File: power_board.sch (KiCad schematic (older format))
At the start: 26 parts, among them J1 Conn_01x01, J10 Conn_01x01, J11 Conn_01x01, J12 Conn_01x01, J13 Conn_01x01, J14 Conn_01x01, J15 Conn_01x01, J16 Conn_01x01, J2 Conn_01x01, J3 Conn_01x01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

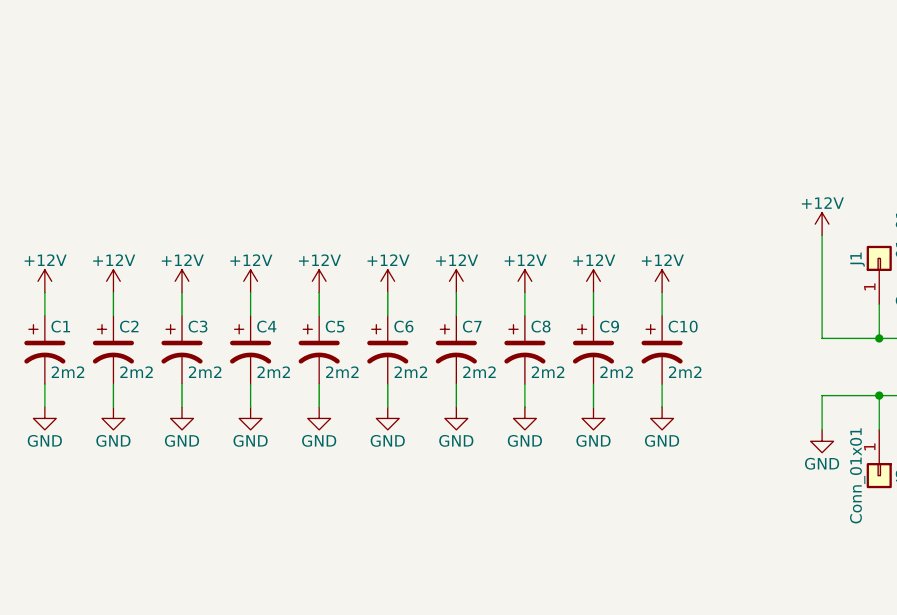
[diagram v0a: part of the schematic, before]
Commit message: add MPN and change footprints
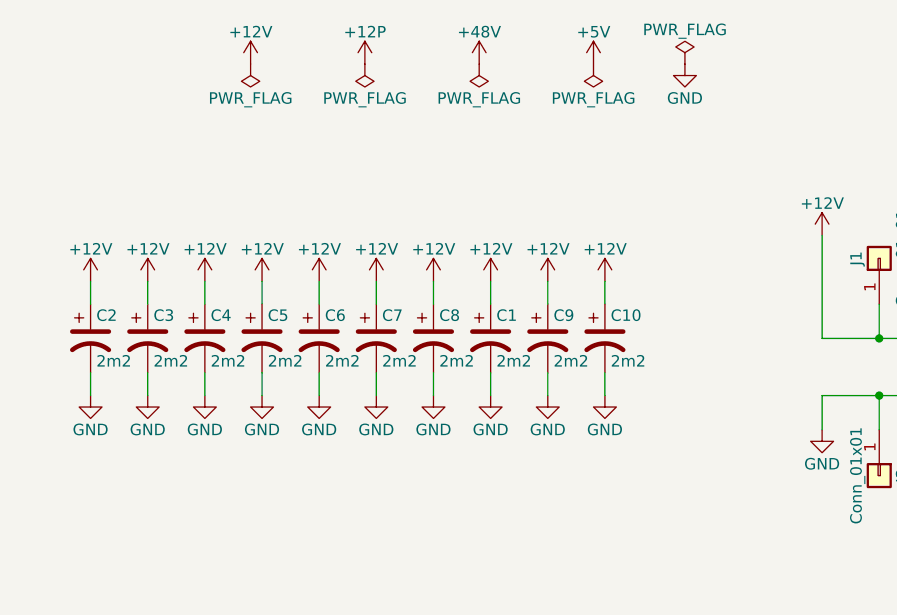
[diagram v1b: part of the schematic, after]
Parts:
- C1: footprint Capacitor_THT:CP_Radial_D10.0mm_P5.00mm -> Capacitor_THT:CP_Radial_D12.5mm_P5.00mm; MPN 565-4315-ND -> 2313329
- C10, C8: footprint Capacitor_THT:CP_Radial_D10.0mm_P5.00mm -> Capacitor_THT:CP_Radial_D12.5mm_P5.00mm; MPN (none) -> 2313329; note 3228 -> (none)
- C2, C3, C5, C6, C7, C9: footprint Capacitor_THT:CP_Radial_D10.0mm_P5.00mm -> Capacitor_THT:CP_Radial_D12.5mm_P5.00mm; MPN (none) -> 2313329
- C4: footprint Capacitors_THT:CP_Radial_D35.0mm_P10.00mm_SnapIn -> Capacitor_THT:CP_Radial_D12.5mm_P5.00mm; MPN (none) -> 2313329; note 3228 -> (none)
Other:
- moved on the sheet: C1

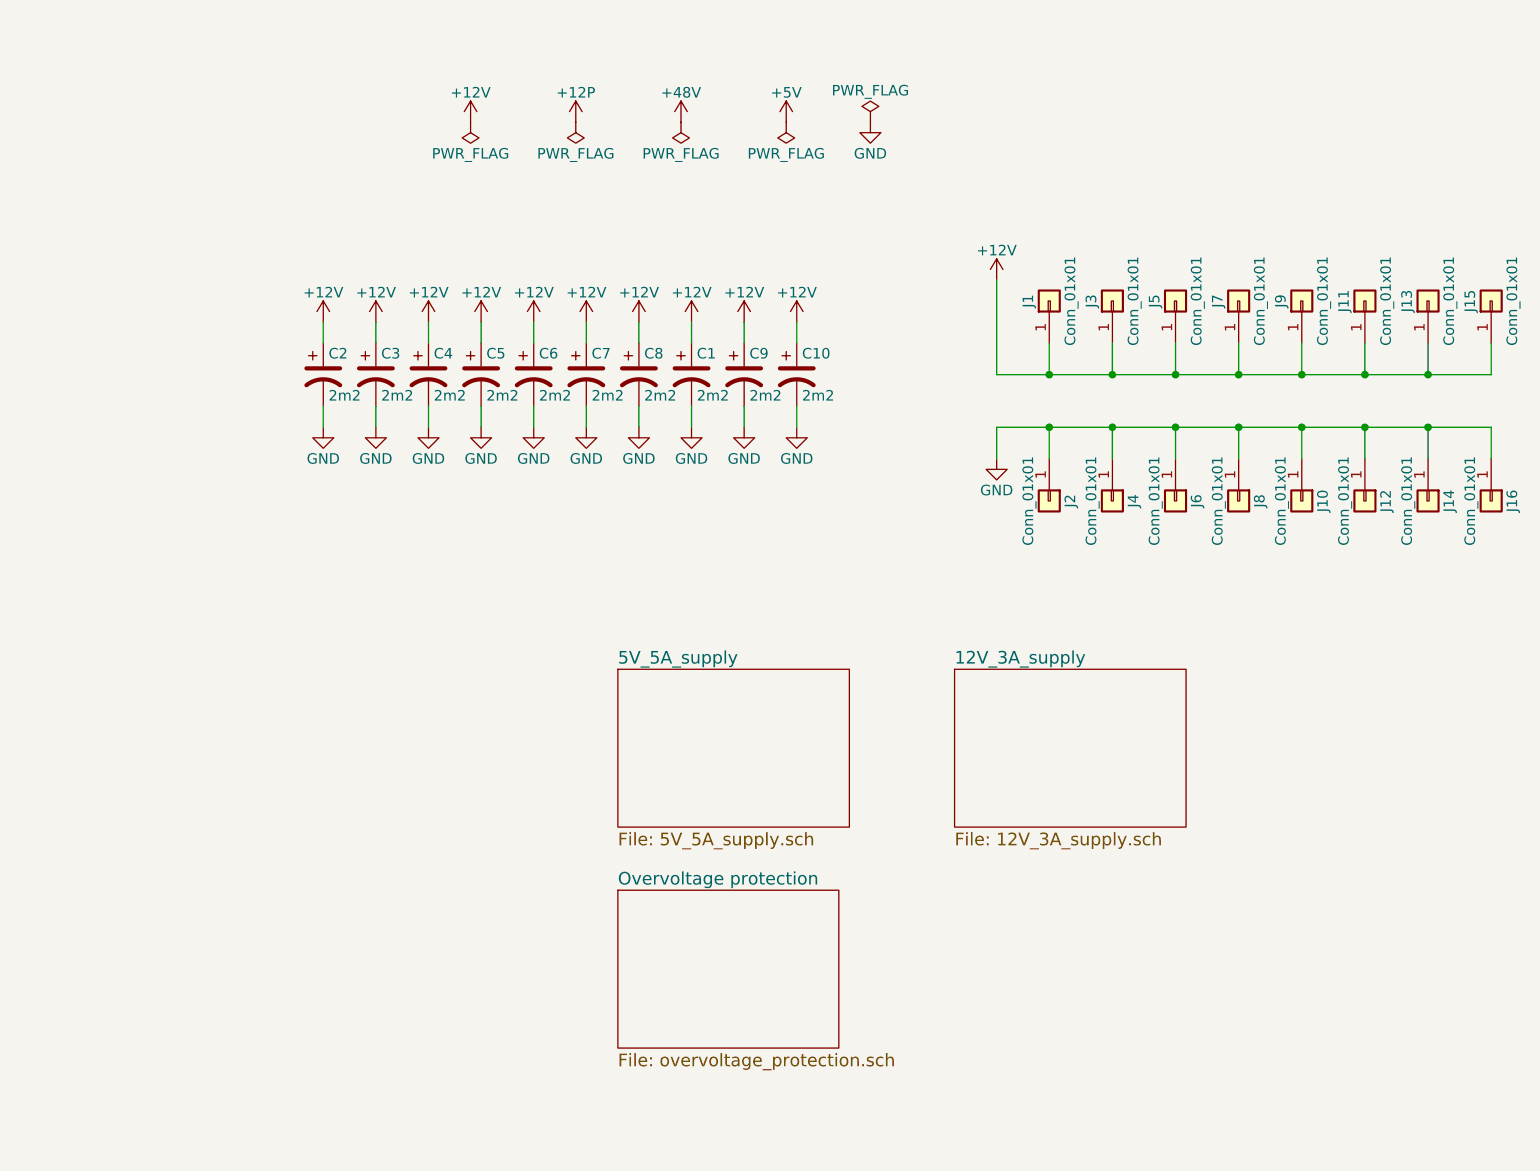
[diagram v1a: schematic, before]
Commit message: 12v 3x_conn added
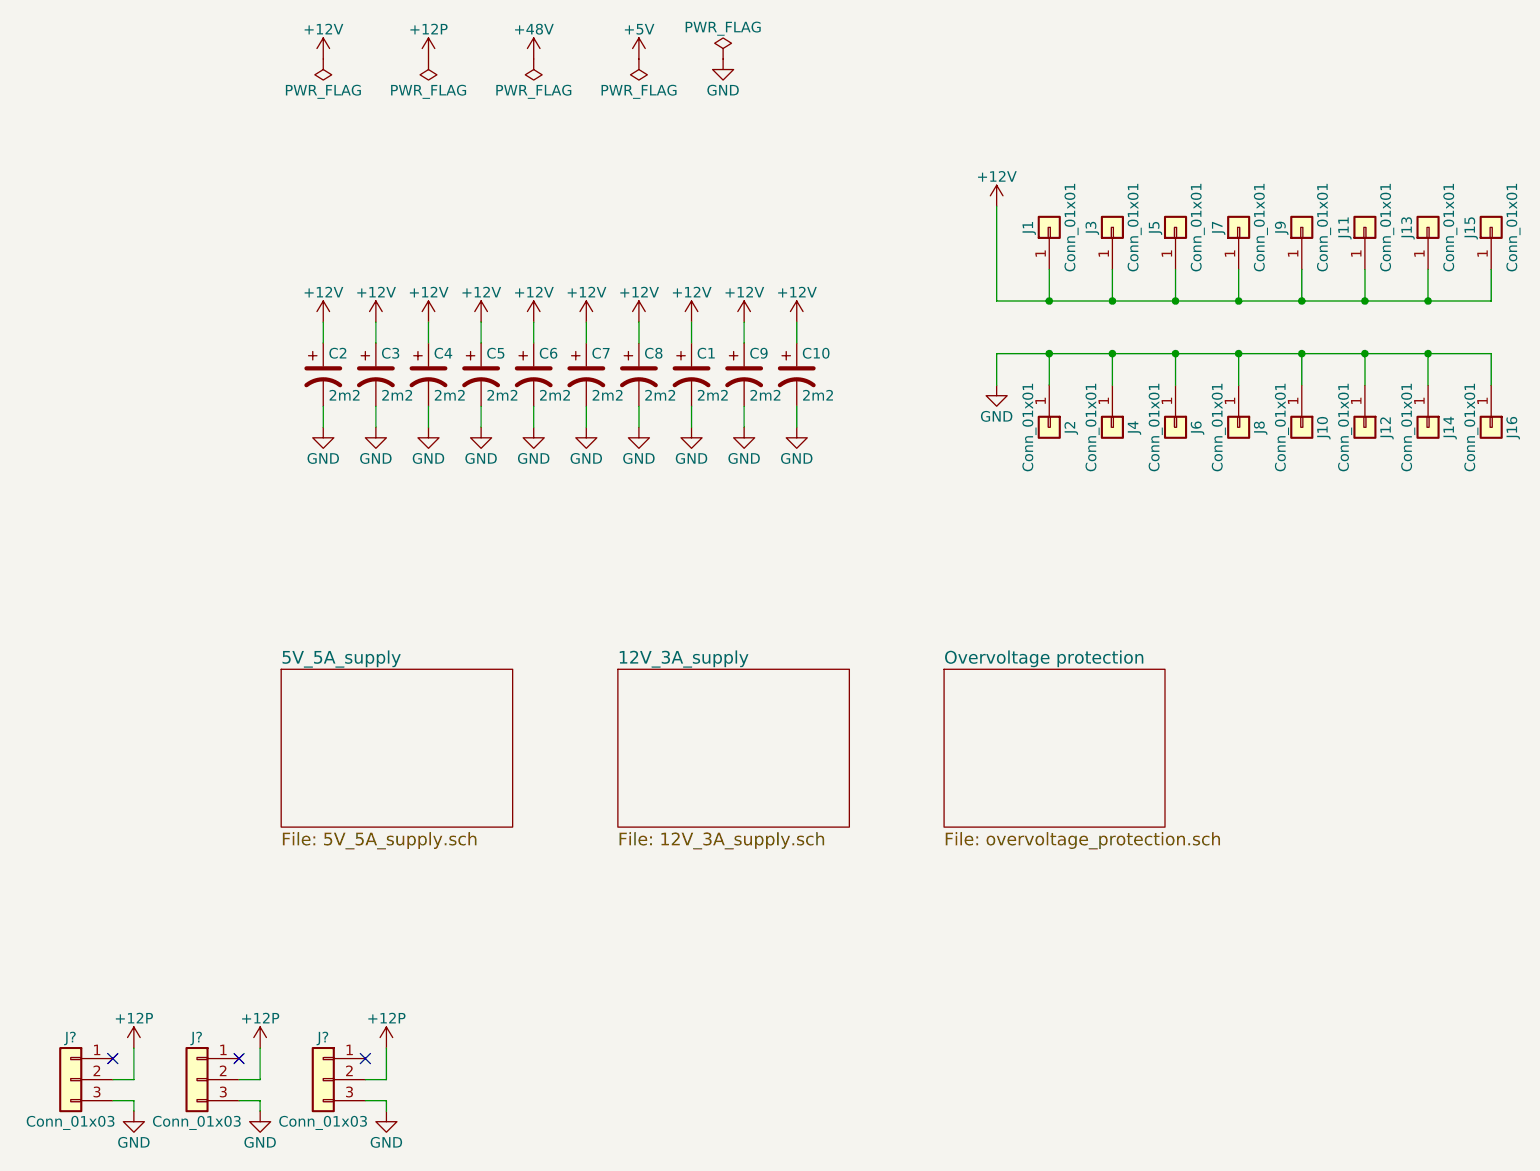
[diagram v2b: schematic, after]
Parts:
- added J? (x3): Conn_01x03, Connector_Molex:Molex_CLIK-Mate_502382-0370_1x03_P1.25mm_Vertical, symbol Conn_01x03
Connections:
- net +12P: now also J?.2 (Pin_2), J?.2 (Pin_2), J?.2 (Pin_2)
- net GND: now also J?.3 (Pin_3), J?.3 (Pin_3), J?.3 (Pin_3)
- no-connect marks 0 -> 3
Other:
- moved on the sheet: J1, J10, J11, J12, J13, J14, J15, J16, J2, J3, J4, J5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

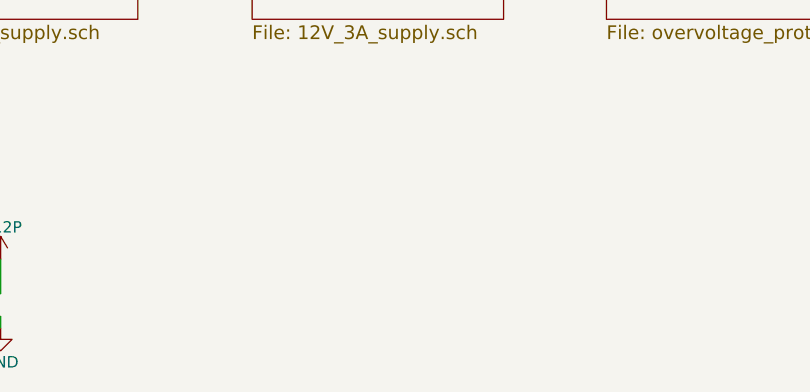
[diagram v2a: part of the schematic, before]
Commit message: mpn was changed
added needed conectors
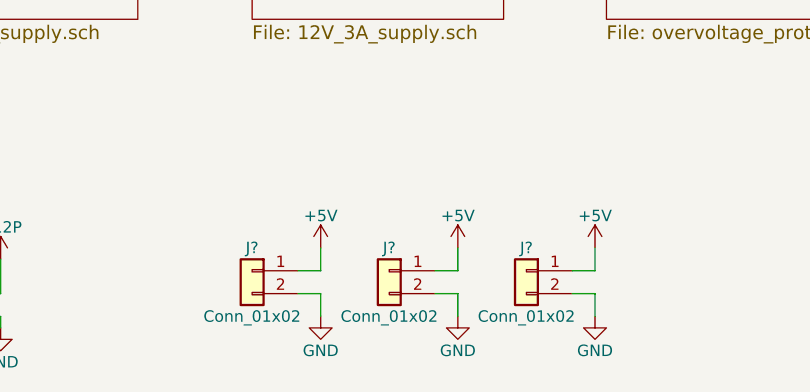
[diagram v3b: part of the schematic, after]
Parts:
- added J? (x3): Conn_01x02, Connector_JST:JST_EH_S02B-EH_1x02_P2.50mm_Horizontal, symbol Conn_01x02
- C1, C10, C2, C3, C4, C5, C6, C7, C8, C9: MPN 2313329 -> EEUFR1C222B
- J? (x3): footprint Connector_Molex:Molex_CLIK-Mate_502382-0370_1x03_P1.25mm_Vertical -> Connector_Molex:Molex_Panelmate_53780-0370_1x03_P1.25mm_Horizontal; MPN 1125359 -> 53261-0371
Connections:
- net +5V: now also J?.1 (Pin_1), J?.1 (Pin_1), J?.1 (Pin_1)
- net GND: now also J?.2 (Pin_2), J?.2 (Pin_2), J?.2 (Pin_2)
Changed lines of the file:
@@
 F 2 "Capacitor_THT:CP_Radial_D12.5mm_P5.00mm" H 4650 2650 50  0001 C CNN
 F 3 "" H 4650 2650 50  0001 C CNN
-F 4 "2313329" H 4650 2650 60  0001 C CNN "MPN"
+F 4 "EEUFR1C222B" H 4650 2650 60  0001 C CNN "MPN"
 	1    4650 2650
 	1    0    0    -1
@@
 F 2 "Capacitor_THT:CP_Radial_D12.5mm_P5.00mm" H 4400 2650 50  0001 C CNN
 F 3 "" H 4400 2650 50  0001 C CNN
-F 4 "2313329" H 4400 2650 60  0001 C CNN "MPN"
+F 4 "EEUFR1C222B" H 4400 2650 60  0001 C CNN "MPN"
 	1    4400 2650
 	1    0    0    -1
@@
 F 2 "Capacitor_THT:CP_Radial_D12.5mm_P5.00mm" H 4150 2650 50  0001 C CNN
 F 3 "" H 4150 2650 50  0001 C CNN
-F 4 "2313329" H 4150 2650 60  0001 C CNN "MPN"
+F 4 "EEUFR1C222B" H 4150 2650 60  0001 C CNN "MPN"
 	1    4150 2650
 	1    0    0    -1
@@
 F 2 "Capacitor_THT:CP_Radial_D12.5mm_P5.00mm" H 3900 2650 50  0001 C CNN
 F 3 "" H 3900 2650 50  0001 C CNN
-F 4 "2313329" H 3900 2650 60  0001 C CNN "MPN"
+F 4 "EEUFR1C222B" H 3900 2650 60  0001 C CNN "MPN"
 	1    3900 2650
 	1    0    0    -1
@@
 F 2 "Capacitor_THT:CP_Radial_D12.5mm_P5.00mm" H 3650 2650 50  0001 C CNN
 F 3 "" H 3650 2650 50  0001 C CNN
-F 4 "2313329" H 3650 2650 60  0001 C CNN "MPN"
+F 4 "EEUFR1C222B" H 3650 2650 60  0001 C CNN "MPN"
 	1    3650 2650
 	1    0    0    -1
@@
 F 2 "Capacitor_THT:CP_Radial_D12.5mm_P5.00mm" H 3400 2650 50  0001 C CNN
 F 3 "" H 3400 2650 50  0001 C CNN
-F 4 "2313329" H 3400 2650 60  0001 C CNN "MPN"
+F 4 "EEUFR1C222B" H 3400 2650 60  0001 C CNN "MPN"
 	1    3400 2650
 	1    0    0    -1
@@
 F 2 "Capacitor_THT:CP_Radial_D12.5mm_P5.00mm" H 3150 2650 50  0001 C CNN
 F 3 "" H 3150 2650 50  0001 C CNN
-F 4 "2313329" H 3150 2650 60  0001 C CNN "MPN"
+F 4 "EEUFR1C222B" H 3150 2650 60  0001 C CNN "MPN"
 	1    3150 2650
 	1    0    0    -1
@@
 F 2 "Capacitor_THT:CP_Radial_D12.5mm_P5.00mm" H 2900 2650 50  0001 C CNN
 F 3 "" H 2900 2650 50  0001 C CNN
-F 4 "2313329" H 2900 2650 60  0001 C CNN "MPN"
+F 4 "EEUFR1C222B" H 2900 2650 60  0001 C CNN "MPN"
 	1    2900 2650
 	1    0    0    -1
@@
 F 2 "Capacitor_THT:CP_Radial_D12.5mm_P5.00mm" H 5150 2650 50  0001 C CNN
 F 3 "" H 5150 2650 50  0001 C CNN
-F 4 "2313329" H 5150 2650 60  0001 C CNN "MPN"
+F 4 "EEUFR1C222B" H 5150 2650 60  0001 C CNN "MPN"
 	1    5150 2650
 	1    0    0    -1
@@
 F 2 "Capacitor_THT:CP_Radial_D12.5mm_P5.00mm" H 4900 2650 50  0001 C CNN
 F 3 "" H 4900 2650 50  0001 C CNN
-F 4 "2313329" H 4900 2650 60  0001 C CNN "MPN"
+F 4 "EEUFR1C222B" H 4900 2650 60  0001 C CNN "MPN"
 	1    4900 2650
 	1    0    0    -1
@@
 F 0 "J?" H 1700 6200 50  0000 C CNN
 F 1 "Conn_01x03" H 1700 5800 50  0000 C CNN
-F 2 "Connector_Molex:Molex_CLIK-Mate_502382-0370_1x03_P1.25mm_Vertical" H 1700 6000 50  0001 C CNN
+F 2 "Connector_Molex:Molex_Panelmate_53780-0370_1x03_P1.25mm_Horizontal" H 1700 6000 50  0001 C CNN
 F 3 "" H 1700 6000 50  0001 C CNN
-F 4 "1125359" H 1700 6000 60  0001 C CNN "MPN"
+F 4 "53261-0371" H 1700 6000 60  0001 C CNN "MPN"
 	1    1700 6000
 	-1   0    0    -1
@@
 F 0 "J?" H 2300 6200 50  0000 C CNN
 F 1 "Conn_01x03" H 2300 5800 50  0000 C CNN
-F 2 "Connector_Molex:Molex_CLIK-Mate_502382-0370_1x03_P1.25mm_Vertical" H 2300 6000 50  0001 C CNN
+F 2 "Connector_Molex:Molex_Panelmate_53780-0370_1x03_P1.25mm_Horizontal" H 2300 6000 50  0001 C CNN
 F 3 "" H 2300 6000 50  0001 C CNN
-F 4 "1125359" H 2300 6000 60  0001 C CNN "MPN"
+F 4 "53261-0371" H 2300 6000 60  0001 C CNN "MPN"
 	1    2300 6000
 	-1   0    0    -1
@@
 F 0 "J?" H 2900 6200 50  0000 C CNN
 F 1 "Conn_01x03" H 2900 5800 50  0000 C CNN
-F 2 "Connector_Molex:Molex_CLIK-Mate_502382-0370_1x03_P1.25mm_Vertical" H 2900 6000 50  0001 C CNN
+F 2 "Connector_Molex:Molex_Panelmate_53780-0370_1x03_P1.25mm_Horizontal" H 2900 6000 50  0001 C CNN
 F 3 "" H 2900 6000 50  0001 C CNN
-F 4 "1125359" H 2900 6000 60  0001 C CNN "MPN"
+F 4 "53261-0371" H 2900 6000 60  0001 C CNN "MPN"
 	1    2900 6000
 	-1   0    0    -1
@@
 Wire Wire Line
 	3200 6100 3200 6150
+$Comp
+L Conn_01x02 J?
+U 1 1 5AB13823
+P 4300 5900
+F 0 "J?" H 4300 6000 50  0000 C CNN
+F 1 "Conn_01x02" H 4300 5700 50  0000 C CNN
+F 2 "Connector_JST:JST_EH_S02B-EH_1x02_P2.50mm_Horizontal" H 4300 5900 50  0001 C CNN
+F 3 "" H 4300 5900 50  0001 C CNN
+F 4 "S2B-EH(LF)(SN)" H 4300 5900 60  0001 C CNN "MPN"
+	1    4300 5900
+	-1   0    0    -1
+$EndComp
+$Comp
+L GND #PWR?
+U 1 1 5AB13AC1
+P 4600 6100
+F 0 "#PWR?" H 4600 5850 50  0001 C CNN
+F 1 "GND" H 4600 5950 50  0000 C CNN
+F 2 "" H 4600 6100 50  0001 C CNN
+F 3 "" H 4600 6100 50  0001 C CNN
+	1    4600 6100
+	1    0    0    -1
+$EndComp
+$Comp
+L GND #PWR?
+U 1 1 5AB13B2C
+P 5200 6100
+F 0 "#PWR?" H 5200 5850 50  0001 C CNN
+F 1 "GND" H 5200 5950 50  0000 C CNN
+F 2 "" H 5200 6100 50  0001 C CNN
+F 3 "" H 5200 6100 50  0001 C CNN
+	1    5200 6100
+	1    0    0    -1
+$EndComp
+$Comp
+L GND #PWR?
+U 1 1 5AB13B97
+P 5800 6100
+F 0 "#PWR?" H 5800 5850 50  0001 C CNN
+F 1 "GND" H 5800 5950 50  0000 C CNN
+F 2 "" H 5800 6100 50  0001 C CNN
+F 3 "" H 5800 6100 50  0001 C CNN
+	1    5800 6100
+	1    0    0    -1
+$EndComp
+$Comp
+L +5V #PWR?
+U 1 1 5AB13D62
+P 4600 5800
+F 0 "#PWR?" H 4600 5650 50  0001 C CNN
+F 1 "+5V" H 4600 5940 50  0000 C CNN
+F 2 "" H 4600 5800 50  0001 C CNN
+F 3 "" H 4600 5800 50  0001 C CNN
+	1    4600 5800
+	1    0    0    -1
+$EndComp
+$Comp
+L +5V #PWR?
+U 1 1 5AB13EED
+P 5200 5800
+F 0 "#PWR?" H 5200 5650 50  0001 C CNN
+F 1 "+5V" H 5200 5940 50  0000 C CNN
+F 2 "" H 5200 5800 50  0001 C CNN
+F 3 "" H 5200 5800 50  0001 C CNN
+	1    5200 5800
+	1    0    0    -1
+$EndComp
+$Comp
+L +5V #PWR?
+U 1 1 5AB13F58
+P 5800 5800
+F 0 "#PWR?" H 5800 5650 50  0001 C CNN
+F 1 "+5V" H 5800 5940 50  0000 C CNN
+F 2 "" H 5800 5800 50  0001 C CNN
+F 3 "" H 5800 5800 50  0001 C CNN
+	1    5800 5800
+	1    0    0    -1
+$EndComp
+Wire Wire Line
+	4500 5900 4600 5900
+Wire Wire Line
+	4600 5900 4600 5800
+Wire Wire Line
+	4500 6000 4600 6000
+Wire Wire Line
+	4600 6000 4600 6100
+Wire Wire Line
+	5100 5900 5200 5900
+Wire Wire Line
+	5200 5900 5200 5800
+Wire Wire Line
+	5100 6000 5200 6000
+Wire Wire Line
+	5200 6000 5200 6100
+Wire Wire Line
+	5700 5900 5800 5900
+Wire Wire Line
+	5800 5900 5800 5800
+Wire Wire Line
+	5700 6000 5800 6000
+Wire Wire Line
+	5800 6000 5800 6100
+$Comp
+L Conn_01x02 J?
+U 1 1 5AB14B61
+P 4900 5900
+F 0 "J?" H 4900 6000 50  0000 C CNN
+F 1 "Conn_01x02" H 4900 5700 50  0000 C CNN
+F 2 "Connector_JST:JST_EH_S02B-EH_1x02_P2.50mm_Horizontal" H 4900 5900 50  0001 C CNN
+F 3 "" H 4900 5900 50  0001 C CNN
+F 4 "S2B-EH(LF)(SN)" H 4900 5900 60  0001 C CNN "MPN"
+	1    4900 5900
+	-1   0    0    -1
+$EndComp
+$Comp
+L Conn_01x02 J?
+U 1 1 5AB14BDA
+P 5500 5900
+F 0 "J?" H 5500 6000 50  0000 C CNN
+F 1 "Conn_01x02" H 5500 5700 50  0000 C CNN
+F 2 "Connector_JST:JST_EH_S02B-EH_1x02_P2.50mm_Horizontal" H 5500 5900 50  0001 C CNN
+F 3 "" H 5500 5900 50  0001 C CNN
+F 4 "S2B-EH(LF)(SN)" H 5500 5900 60  0001 C CNN "MPN"
+	1    5500 5900
+	-1   0    0    -1
+$EndComp
 $EndSCHEMATC
